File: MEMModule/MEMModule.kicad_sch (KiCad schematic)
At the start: 5 parts

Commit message: Add revision number to MEMModule PCB
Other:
- title: Turtle16: MEM -> Turtle16: MEM + RAM
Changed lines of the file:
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@@
   (paper "USLetter")
   (title_block
-    (title "Turtle16: MEM")
+    (title "Turtle16: MEM + RAM")
     (date "2022-04-12")
-    (rev "A")
+    (rev "A (584b6b4f)")
     (comment 4 "MEM Pipeline Stage and Computer Memory")
   )

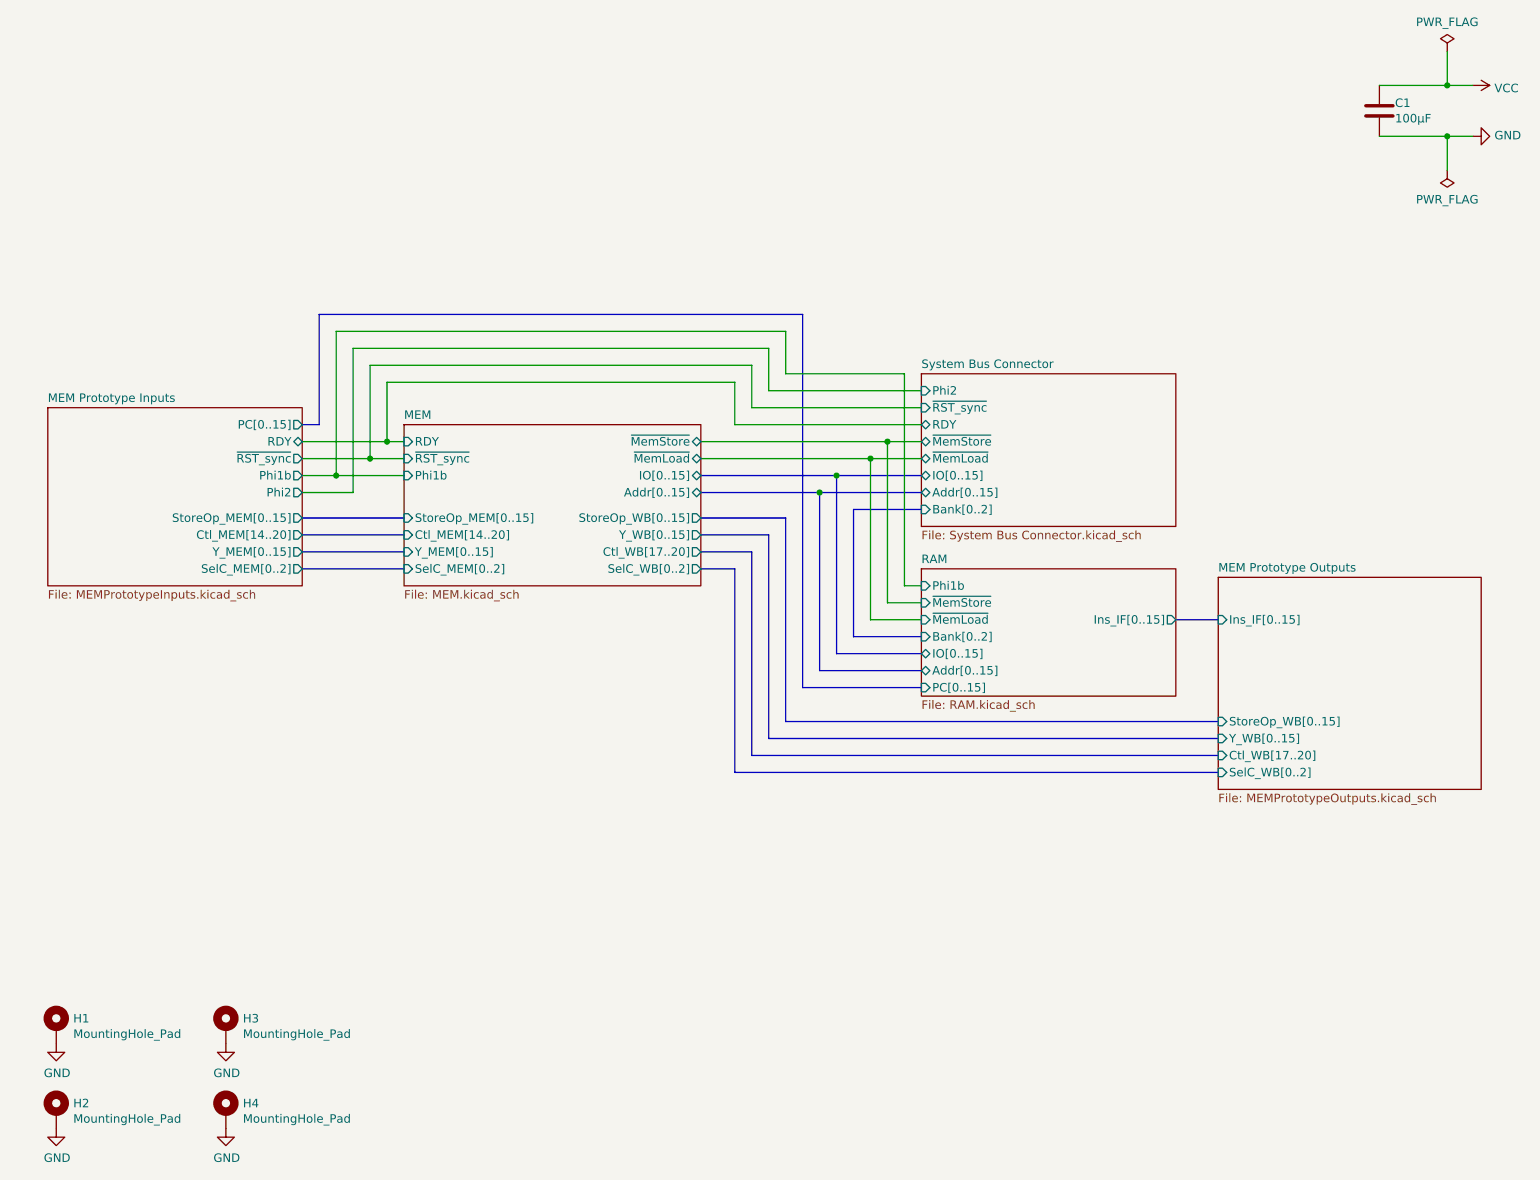
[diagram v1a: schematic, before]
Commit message: Use 74HC173 for Bank select register because it can reset to zero
Having the memory bank reset to a known value when power is applied is
going to be very convenient
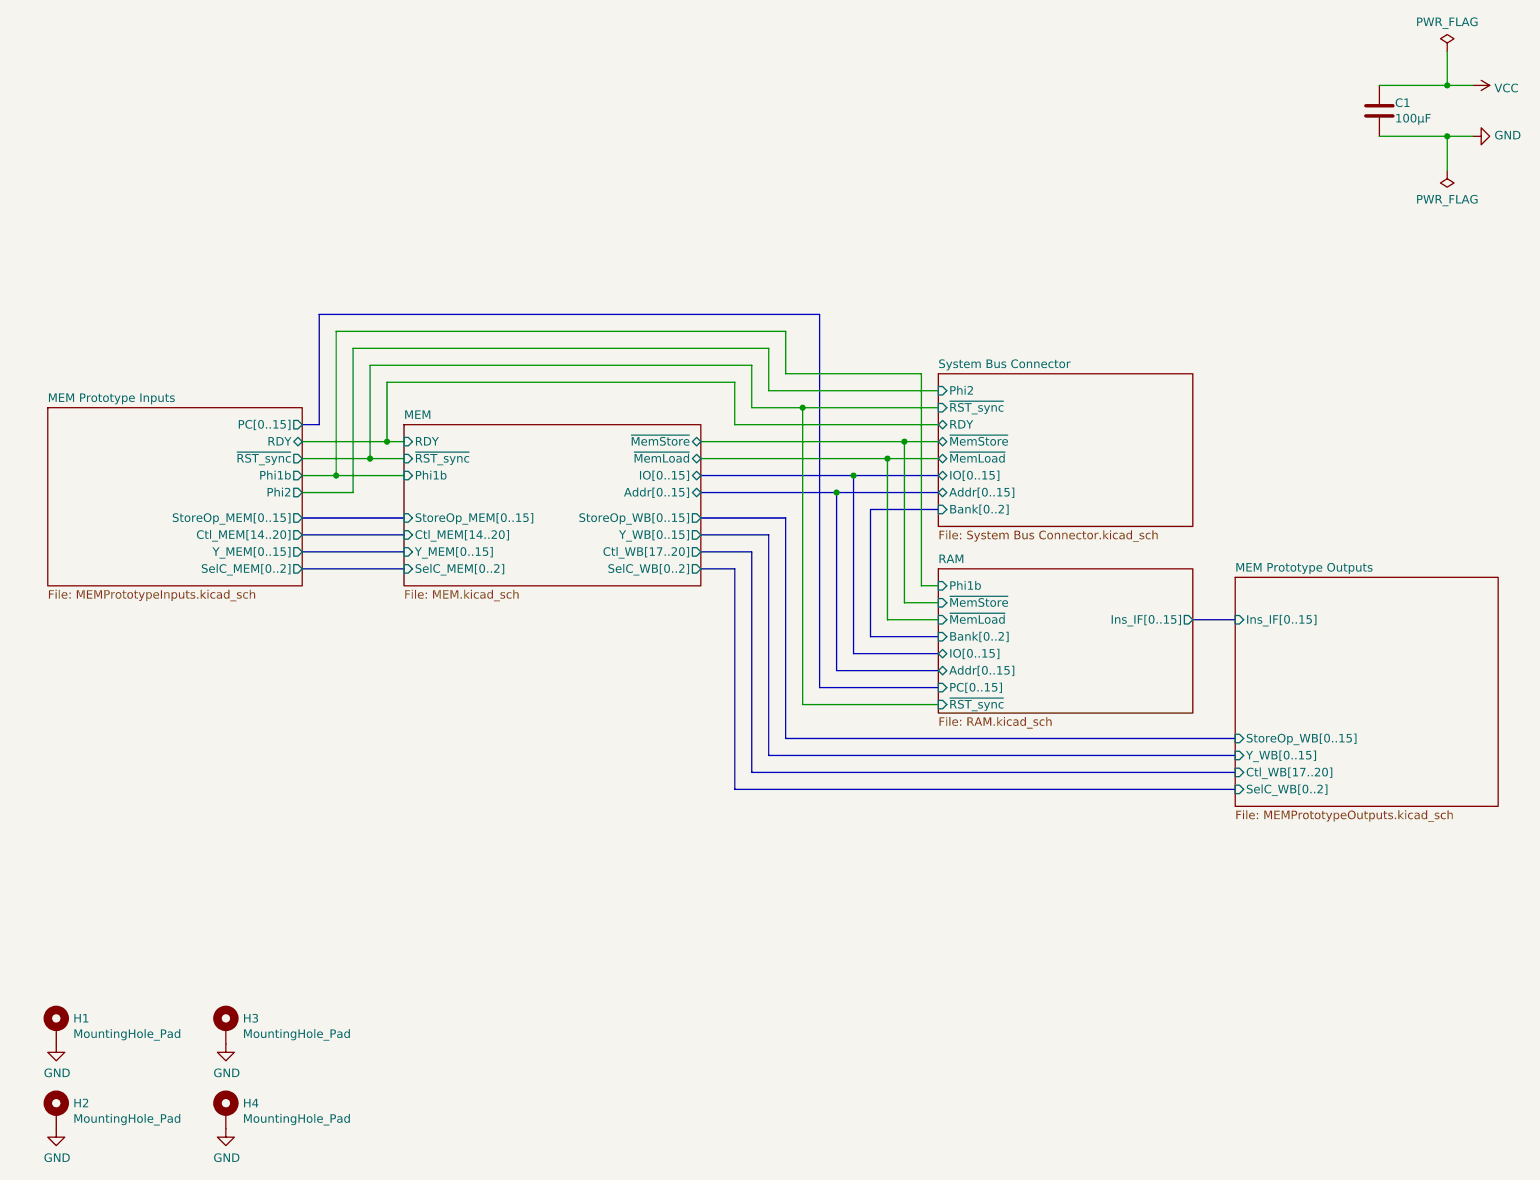
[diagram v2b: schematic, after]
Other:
- sheet RAM ports: added ~{RST_sync}; removed none

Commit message: MEMModule: Add FLUSH_IF input
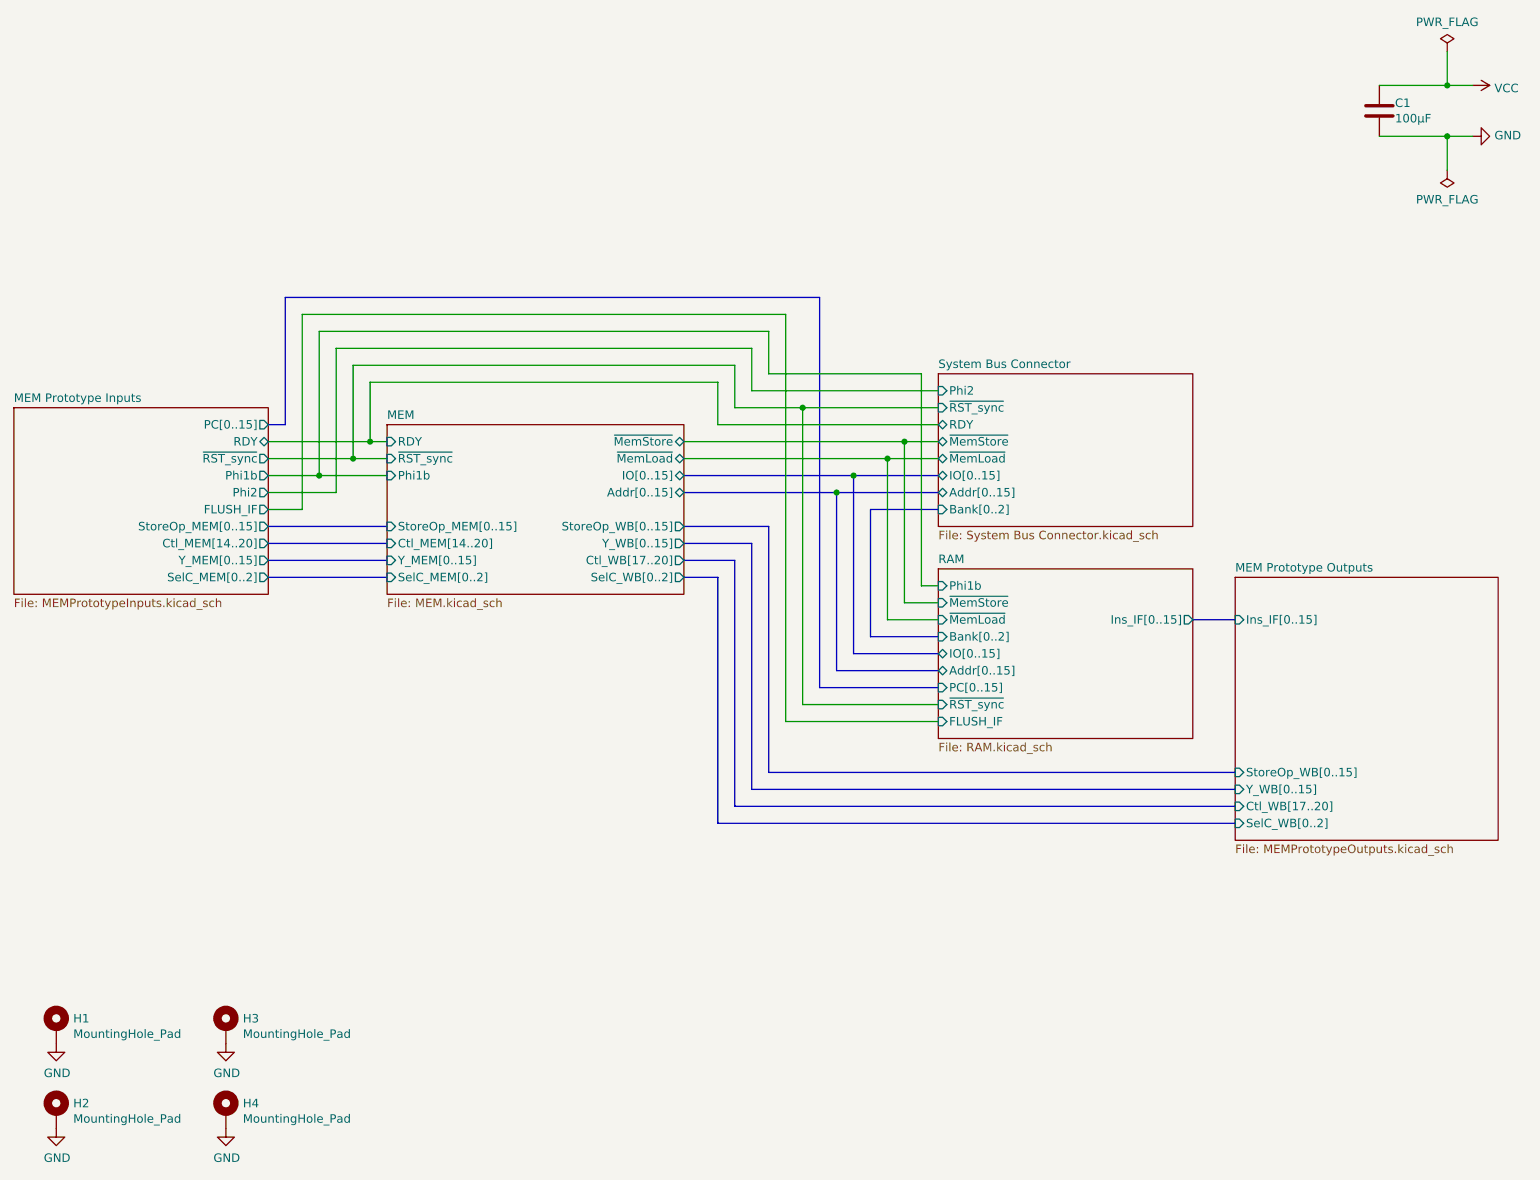
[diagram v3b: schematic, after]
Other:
- sheet MEM Prototype Inputs ports: added FLUSH_IF; removed none
- sheet RAM ports: added FLUSH_IF; removed none

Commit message: MEMModule now has ROM on Bank 0 again
The idea of having a system with no built-in ROM is turning out to be more
complicated than I expected. The boot device is additional complexity that
I'm now reluctant to take on. It's still, after months, not fully designed
and prototyped. Let's eliminate the need for this entire module by having
the computer run from ROM on boot.

The benefits of a ROM-less system are more difficult to achieve than
expected. The device would need a fast sixteen bit ALU chip as in the
program counter. Using simple counters like the 74F161 would bottleneck the
counting sopeed at 12.5MHz and the boot device provides no effective speed
benefit.

Further, the entire scheme is a performance optimization for a machine that
hasn't even been fully constructed yet. I can take on optimization work
later.

So this change sticks a pair of fast ROMS into MEM on Bank zero. A program
can set the Bank register to something else in order to map the built-in
RAM to instruction memory instead.

Also, update MEMModule for KiCad 7.
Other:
- removed sheet RAM
- added sheet Memory (Memory.kicad_sch)

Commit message: MEMModule: update description text
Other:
- title: Turtle16: MEM + RAM -> Turtle16: MEM, RAM, ROM
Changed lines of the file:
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@@
   (paper "USLetter")
   (title_block
-    (title "Turtle16: MEM + RAM")
+    (title "Turtle16: MEM, RAM, ROM")
     (date "2023-03-22")
     (rev "B")
